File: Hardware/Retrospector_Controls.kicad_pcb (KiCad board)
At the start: 2 copper layers, 60 x 110 mm, 23 parts, among them J1 Audio_In_L, J10 Feedback_CV, J11 Audio_In_R, J12 Audio_Out_R, J13 Audio_Out_L, J2 Delay_CV_L, J3 Conn_01x08_Female, J4 Conn_01x08_Female, J5 Conn_01x08_Female, J6 Conn_01x08_Female, J7 Mix_CV, J8 Delay_CV_R, J9 Clock

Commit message: Renamed project files; work on panel PCB and 3d Models
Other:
- board text added: "Retrospector Controls v1 Mountjoy Modular"
- board text removed: "Alligator Controls v1 Mountjoy Modular"
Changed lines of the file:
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@@
   )
   (gr_line (start 130 50) (end 130 160) (layer Dwgs.User) (width 0.05))
-  (gr_text "Alligator Controls v1\nMountjoy Modular" (at 130.9 53.6) (layer B.SilkS)
+  (gr_text "Retrospector Controls v1\nMountjoy Modular" (at 130.9 53.6) (layer B.SilkS)
     (effects (font (size 1.5 1.5) (thickness 0.3)) (justify mirror))
   )

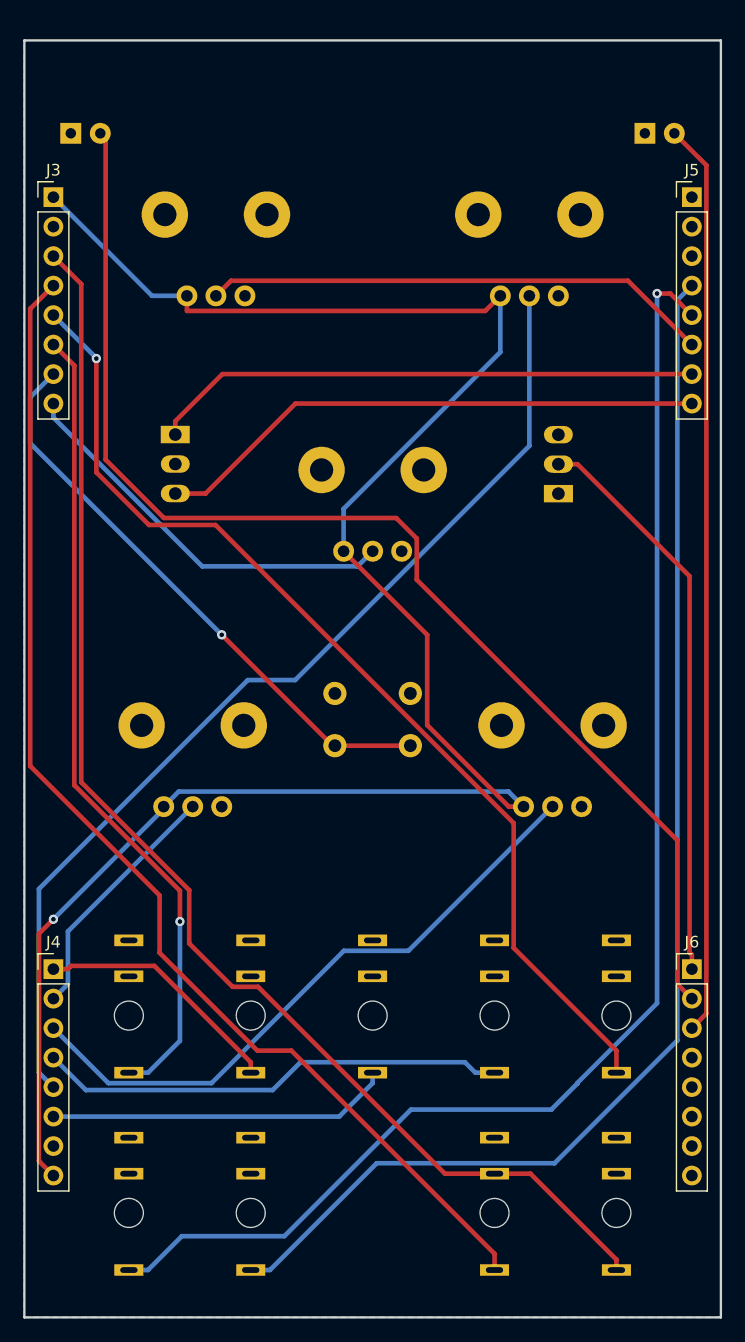
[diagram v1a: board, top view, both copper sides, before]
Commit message: Panel and Control PCB Updates
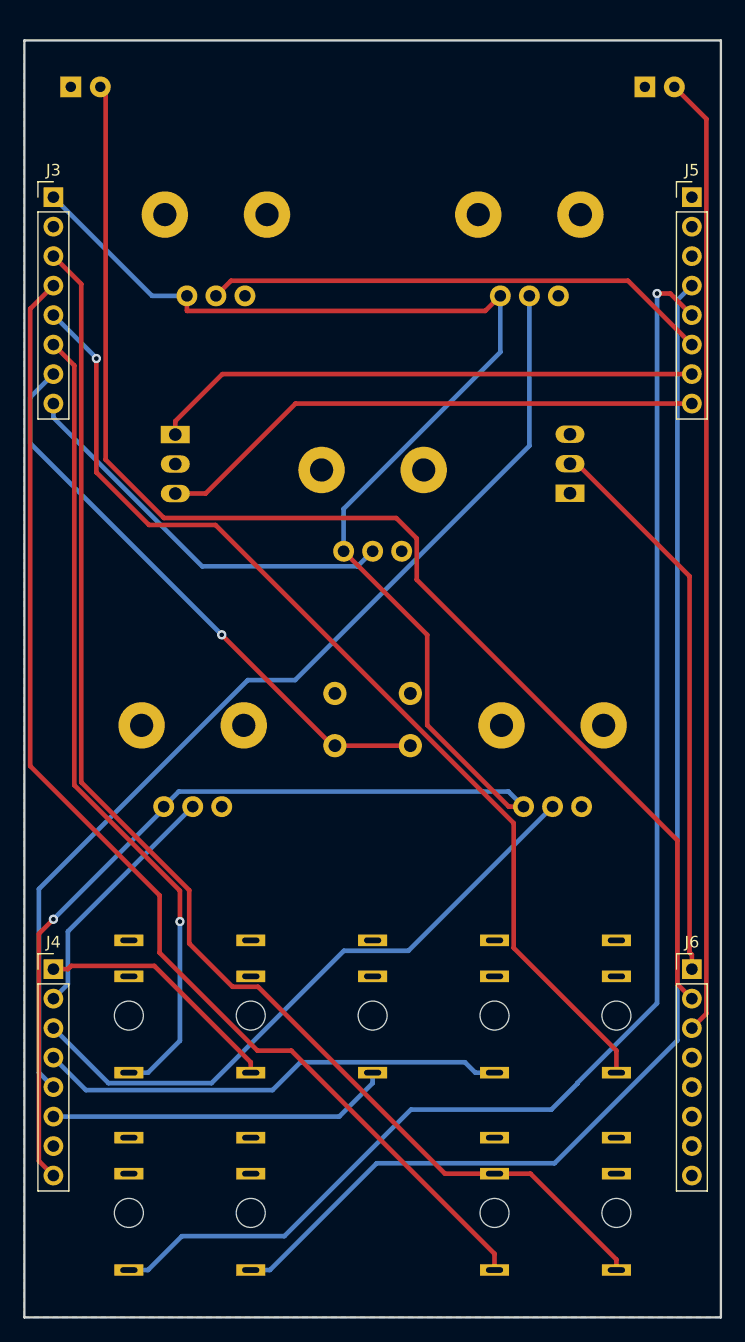
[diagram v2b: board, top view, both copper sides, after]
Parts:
- moved D1 4.00 mm to (153.4, 54.0)
- moved D2 4.00 mm to (104.0, 54.0)
- moved FXTYPE1 1.00 mm to (147.0, 89.0)
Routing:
- net /LED2: track 107.4 -> 112.4 mm
- net /LED1: track 78.7 -> 82.7 mm
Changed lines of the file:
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@@
     (thickness 1.6)
     (drawings 6)
-    (tracks 141)
+    (tracks 143)
     (zones 0)
     (modules 23)
@@
   )
   (module Custom_Footprints:SPDTSubMiniature (layer B.Cu)
-    (at 146 89.04 90)
+    (at 147 89 90)
     (descr "SPDT Sub Miniature Switch")
     (tags "Switch SPDT")
@@
   )
   (module LEDs:LED_D3.0mm (layer B.Cu)
-    (at 104 58)
+    (at 104 54)
     (descr "LED, diameter 3.0mm, 2 pins")
     (tags "LED diameter 3.0mm 2 pins")
@@
   )
   (module LEDs:LED_D3.0mm (layer B.Cu)
-    (at 153.45 58)
+    (at 153.45 54)
     (descr "LED, diameter 3.0mm, 2 pins")
     (tags "LED diameter 3.0mm 2 pins")
@@
   (segment (start 133.079999 128.420001) (end 127.522001 128.420001) (width 0.4) (layer B.Cu) (net 22))
   (segment (start 145.5 116) (end 133.079999 128.420001) (width 0.4) (layer B.Cu) (net 22) (status 10))
-  (segment (start 158.750001 133.829999) (end 157.5 135.08) (width 0.4) (layer F.Cu) (net 23) (status 20))
-  (segment (start 155.99 58) (end 158.750001 60.750001) (width 0.4) (layer F.Cu) (net 23) (status 10))
-  (segment (start 158.750001 60.750001) (end 158.750001 133.829999) (width 0.4) (layer F.Cu) (net 23))
-  (segment (start 107.000001 58.460001) (end 106.54 58) (width 0.4) (layer F.Cu) (net 24) (status 30))
-  (segment (start 107.000001 86.11416) (end 107.000001 58.460001) (width 0.4) (layer F.Cu) (net 24) (status 20))
+  (segment (start 158.750001 133.829999) (end 157.5 135.08) (width 0.4) (layer F.Cu) (net 23))
+  (segment (start 155.99 54) (end 158.750001 56.760001) (width 0.4) (layer F.Cu) (net 23))
+  (segment (start 158.750001 56.760001) (end 158.750001 133.829999) (width 0.4) (layer F.Cu) (net 23))
+  (segment (start 106.54 54) (end 107 54) (width 0.4) (layer F.Cu) (net 24))
+  (segment (start 106.54 54) (end 106.54 54.54) (width 0.4) (layer F.Cu) (net 24))
+  (segment (start 107.000001 86.11416) (end 107.000001 54.460001) (width 0.4) (layer F.Cu) (net 24))
+  (segment (start 112.023651 91.13781) (end 107.000001 86.11416) (width 0.4) (layer F.Cu) (net 24))
   (segment (start 132.03781 91.13781) (end 112.023651 91.13781) (width 0.4) (layer F.Cu) (net 24))
-  (segment (start 157.5 132.54) (end 156.249999 131.289999) (width 0.4) (layer F.Cu) (net 24) (status 10))
+  (segment (start 156.249999 131.289999) (end 156.249999 118.902001) (width 0.4) (layer F.Cu) (net 24))
+  (segment (start 107.000001 54.460001) (end 106.54 54) (width 0.4) (layer F.Cu) (net 24))
+  (segment (start 157.5 132.54) (end 156.249999 131.289999) (width 0.4) (layer F.Cu) (net 24))
+  (segment (start 133.800001 92.900001) (end 132.03781 91.13781) (width 0.4) (layer F.Cu) (net 24))
   (segment (start 156.249999 118.902001) (end 133.800001 96.452003) (width 0.4) (layer F.Cu) (net 24))
-  (segment (start 112.023651 91.13781) (end 107.000001 86.11416) (width 0.4) (layer F.Cu) (net 24))
-  (segment (start 133.800001 92.900001) (end 132.03781 91.13781) (width 0.4) (layer F.Cu) (net 24))
-  (segment (start 156.249999 131.289999) (end 156.249999 118.902001) (width 0.4) (layer F.Cu) (net 24))
   (segment (start 133.800001 96.452003) (end 133.800001 92.900001) (width 0.4) (layer F.Cu) (net 24))
   (segment (start 115.31792 95.300001) (end 102.5 82.482081) (width 0.4) (layer B.Cu) (net 25))

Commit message: Final changes to PCBs for manufacture
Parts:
- moved Delay_Pot_L1 0.50 mm to (141.5, 72.0)
- moved Delay_Pot_R1 0.50 mm to (113.5, 72.0)
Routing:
- net /DELAY_POT_R: track 43.8 -> 44.3 mm
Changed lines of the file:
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@@
       (drillshape 0)
       (scaleselection 1)
-      (outputdirectory "Gerbers/Components/"))
+      (outputdirectory "Gerbers/Controls/"))
   )
   (net 0 "")
@@
   )
   (module Custom_Footprints:Alpha_9mm_Potentiometer (layer B.Cu)
-    (at 114 72 90)
+    (at 113.5 72 90)
     (descr "Potentiometer, horizontally mounted, Omeg PC16PU, Omeg PC16PU, Omeg PC16PU, Vishay/Spectrol 248GJ/249GJ Single, Vishay/Spectrol 248GJ/249GJ Single, Vishay/Spectrol 248GJ/249GJ Single, Vishay/Spectrol 248GH/249GH Single, Vishay/Spectrol 148/149 Single, Vishay/Spectrol 148/149 Single, Vishay/Spectrol 148/149 Single, Vishay/Spectrol 148A/149A Single with mounting plates, Vishay/Spectrol 148/149 Double, Vishay/Spectrol 148A/149A Double with mounting plates, Piher PC-16 Single, Piher PC-16 Single, Piher PC-16 Single, Piher PC-16SV Single, Piher PC-16 Double, Piher PC-16 Triple, Piher T16H Single, Piher T16L Single, Piher T16H Double, Alps RK163 Single, Alps RK163 Double, Alps RK097 Single, Alps RK097 Double, Bourns PTV09A-2 Single with mounting sleve Single, Bourns PTV09A-1 with mounting sleve Single, Bourns PRS11S Single, Alps RK09K Single with mounting sleve Single, Alps RK09K with mounting sleve Single, http://www.alps.com/prod/info/E/HTML/Potentiometer/RotaryPotentiometers/RK09K/RK09D1130C1B.html")
     (tags "Potentiometer horizontal  Omeg PC16PU  Omeg PC16PU  Omeg PC16PU  Vishay/Spectrol 248GJ/249GJ Single  Vishay/Spectrol 248GJ/249GJ Single  Vishay/Spectrol 248GJ/249GJ Single  Vishay/Spectrol 248GH/249GH Single  Vishay/Spectrol 148/149 Single  Vishay/Spectrol 148/149 Single  Vishay/Spectrol 148/149 Single  Vishay/Spectrol 148A/149A Single with mounting plates  Vishay/Spectrol 148/149 Double  Vishay/Spectrol 148A/149A Double with mounting plates  Piher PC-16 Single  Piher PC-16 Single  Piher PC-16 Single  Piher PC-16SV Single  Piher PC-16 Double  Piher PC-16 Triple  Piher T16H Single  Piher T16L Single  Piher T16H Double  Alps RK163 Single  Alps RK163 Double  Alps RK097 Single  Alps RK097 Double  Bourns PTV09A-2 Single with mounting sleve Single  Bourns PTV09A-1 with mounting sleve Single  Bourns PRS11S Single  Alps RK09K Single with mounting sleve Single  Alps RK09K with mounting sleve Single")
@@
   )
   (module Custom_Footprints:Alpha_9mm_Potentiometer (layer B.Cu)
-    (at 141 72 90)
+    (at 141.5 72 90)
     (descr "Potentiometer, horizontally mounted, Omeg PC16PU, Omeg PC16PU, Omeg PC16PU, Vishay/Spectrol 248GJ/249GJ Single, Vishay/Spectrol 248GJ/249GJ Single, Vishay/Spectrol 248GJ/249GJ Single, Vishay/Spectrol 248GH/249GH Single, Vishay/Spectrol 148/149 Single, Vishay/Spectrol 148/149 Single, Vishay/Spectrol 148/149 Single, Vishay/Spectrol 148A/149A Single with mounting plates, Vishay/Spectrol 148/149 Double, Vishay/Spectrol 148A/149A Double with mounting plates, Piher PC-16 Single, Piher PC-16 Single, Piher PC-16 Single, Piher PC-16SV Single, Piher PC-16 Double, Piher PC-16 Triple, Piher T16H Single, Piher T16L Single, Piher T16H Double, Alps RK163 Single, Alps RK163 Double, Alps RK097 Single, Alps RK097 Double, Bourns PTV09A-2 Single with mounting sleve Single, Bourns PTV09A-1 with mounting sleve Single, Bourns PRS11S Single, Alps RK09K Single with mounting sleve Single, Alps RK09K with mounting sleve Single, http://www.alps.com/prod/info/E/HTML/Potentiometer/RotaryPotentiometers/RK09K/RK09D1130C1B.html")
     (tags "Potentiometer horizontal  Omeg PC16PU  Omeg PC16PU  Omeg PC16PU  Vishay/Spectrol 248GJ/249GJ Single  Vishay/Spectrol 248GJ/249GJ Single  Vishay/Spectrol 248GJ/249GJ Single  Vishay/Spectrol 248GH/249GH Single  Vishay/Spectrol 148/149 Single  Vishay/Spectrol 148/149 Single  Vishay/Spectrol 148/149 Single  Vishay/Spectrol 148A/149A Single with mounting plates  Vishay/Spectrol 148/149 Double  Vishay/Spectrol 148A/149A Double with mounting plates  Piher PC-16 Single  Piher PC-16 Single  Piher PC-16 Single  Piher PC-16SV Single  Piher PC-16 Double  Piher PC-16 Triple  Piher T16H Single  Piher T16L Single  Piher T16H Double  Alps RK163 Single  Alps RK163 Double  Alps RK097 Single  Alps RK097 Double  Bourns PTV09A-2 Single with mounting sleve Single  Bourns PTV09A-1 with mounting sleve Single  Bourns PRS11S Single  Alps RK09K Single with mounting sleve Single  Alps RK09K with mounting sleve Single")
@@
   (segment (start 134.700001 108.972793) (end 134.700001 101.200001) (width 0.4) (layer F.Cu) (net 2))
   (segment (start 143 116) (end 141.727208 116) (width 0.4) (layer F.Cu) (net 2) (status 10))
-  (segment (start 141 76.847998) (end 141 72) (width 0.4) (layer B.Cu) (net 2) (status 20))
-  (segment (start 127.5 90.347998) (end 141 76.847998) (width 0.4) (layer B.Cu) (net 2))
-  (segment (start 127.5 94) (end 127.5 90.347998) (width 0.4) (layer B.Cu) (net 2) (status 10))
   (segment (start 101.249999 126.950001) (end 102.5 125.7) (width 0.4) (layer F.Cu) (net 2))
   (segment (start 102.5 147.78) (end 101.249999 146.529999) (width 0.4) (layer F.Cu) (net 2) (status 10))
@@
   (segment (start 111 72) (end 102.5 63.5) (width 0.4) (layer B.Cu) (net 2) (status 20))
   (segment (start 114 72) (end 111 72) (width 0.4) (layer B.Cu) (net 2) (status 10))
-  (segment (start 114.027209 73.300001) (end 139.699999 73.300001) (width 0.4) (layer F.Cu) (net 2))
-  (segment (start 139.699999 73.300001) (end 141 72) (width 0.4) (layer F.Cu) (net 2) (status 20))
-  (segment (start 114 73.272792) (end 114.027209 73.300001) (width 0.4) (layer F.Cu) (net 2))
-  (segment (start 114 72) (end 114 73.272792) (width 0.4) (layer F.Cu) (net 2) (status 10))
   (segment (start 113.300001 114.699999) (end 112 116) (width 0.4) (layer B.Cu) (net 2) (status 20))
   (segment (start 141.699999 114.699999) (end 113.300001 114.699999) (width 0.4) (layer B.Cu) (net 2))
   (segment (start 143 116) (end 141.699999 114.699999) (width 0.4) (layer B.Cu) (net 2) (status 10))
+  (segment (start 139.699999 73.300001) (end 141 72) (width 0.4) (layer F.Cu) (net 2))
+  (segment (start 114.027209 73.300001) (end 139.699999 73.300001) (width 0.4) (layer F.Cu) (net 2))
+  (segment (start 113.5 72) (end 113.5 72.772792) (width 0.4) (layer F.Cu) (net 2))
+  (segment (start 113.5 72.772792) (end 114.027209 73.300001) (width 0.4) (layer F.Cu) (net 2))
+  (segment (start 141.5 72) (end 141.5 76.347998) (width 0.4) (layer B.Cu) (net 2))
+  (segment (start 127.5 90.347998) (end 127.5 94) (width 0.4) (layer B.Cu) (net 2))
+  (segment (start 141.5 76.347998) (end 127.5 90.347998) (width 0.4) (layer B.Cu) (net 2))
   (segment (start 157.5 128.75) (end 157.5 130) (width 0.4) (layer F.Cu) (net 3) (status 20))
   (segment (start 157.3 96.15) (end 157.3 128.55) (width 0.4) (layer F.Cu) (net 3))
@@
   (segment (start 116.465818 91.73782) (end 110.73782 91.73782) (width 0.4) (layer F.Cu) (net 15))
   (segment (start 142.150001 117.422003) (end 116.465818 91.73782) (width 0.4) (layer F.Cu) (net 15))
-  (segment (start 102.5 140.16) (end 101.249999 138.909999) (width 0.4) (layer B.Cu) (net 16) (status 10))
-  (segment (start 101.249999 123.097999) (end 119.247999 105.099999) (width 0.4) (layer B.Cu) (net 16))
-  (segment (start 143.5 84.924002) (end 143.5 72) (width 0.4) (layer B.Cu) (net 16) (status 20))
-  (segment (start 119.247999 105.099999) (end 123.324003 105.099999) (width 0.4) (layer B.Cu) (net 16))
-  (segment (start 101.249999 138.909999) (end 101.249999 123.097999) (width 0.4) (layer B.Cu) (net 16))
-  (segment (start 123.324003 105.099999) (end 143.5 84.924002) (width 0.4) (layer B.Cu) (net 16))
+  (segment (start 101.249999 138.909999) (end 102.5 140.16) (width 0.4) (layer B.Cu) (net 16))
+  (segment (start 144 84.424002) (end 123.324003 105.099999) (width 0.4) (layer B.Cu) (net 16))
+  (segment (start 144 72) (end 144 84.424002) (width 0.4) (layer B.Cu) (net 16))
+  (segment (start 123.324003 105.099999) (end 119.247999 105.099999) (width 0.4) (layer B.Cu) (net 16))
+  (segment (start 119.247999 105.099999) (end 101.249999 123.097999) (width 0.4) (layer B.Cu) (net 16))
+  (segment (start 101.249999 123.097999) (end 101.249999 138.909999) (width 0.4) (layer B.Cu) (net 16))
   (via (at 113.4 125.9) (size 0.8) (drill 0.4) (layers F.Cu B.Cu) (net 17))
   (segment (start 104.29999 77.99999) (end 102.5 76.2) (width 0.4) (layer F.Cu) (net 17) (status 20))
@@
   (segment (start 109 138.92) (end 110.65 138.92) (width 0.4) (layer B.Cu) (net 17) (status 10))
   (segment (start 110.65 138.92) (end 113.4 136.17) (width 0.4) (layer B.Cu) (net 17))
-  (segment (start 117.800001 70.699999) (end 116.5 72) (width 0.4) (layer F.Cu) (net 18) (status 20))
-  (segment (start 151.999999 70.699999) (end 117.800001 70.699999) (width 0.4) (layer F.Cu) (net 18))
-  (segment (start 157.5 76.2) (end 151.999999 70.699999) (width 0.4) (layer F.Cu) (net 18) (status 10))
+  (segment (start 151.999999 70.699999) (end 157.5 76.2) (width 0.4) (layer F.Cu) (net 18))
+  (segment (start 116 72) (end 117.300001 70.699999) (width 0.4) (layer F.Cu) (net 18))
+  (segment (start 117.300001 70.699999) (end 151.999999 70.699999) (width 0.4) (layer F.Cu) (net 18))
   (segment (start 103.750001 126.749999) (end 114.5 116) (width 0.4) (layer B.Cu) (net 19) (status 20))
   (segment (start 103.750001 131.289999) (end 103.750001 126.749999) (width 0.4) (layer B.Cu) (net 19))

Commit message: Updates to control and panel PCBs
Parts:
- removed FXTYPE1: SW_SPST, Custom_Footprints:SPDTSubMiniature
- added C1: 47uF, Capacitors_SMD:CP_Elec_5x5.8, F.Cu at (146.8, 54.2)
- added D3: LED_RGBA, Custom_Footprints:LED_RGB_PLCC4, B.Cu at (130.0, 102.2)
- added FILTER_MODE1: SW_SPDT_MSM, Custom_Footprints:SPDT_SubMiniature_Aligned, B.Cu at (130.1, 110.3)
- added J14: Filter, Custom_Footprints:THONKICONN_hole, B.Cu at (130.1, 127.1)
- added LOCK1: SW_Push, Custom_Footprints:SW_PUSH_6mm_aligned, B.Cu at (130.1, 65.6)
- added R1: 3k3, Resistors_SMD:R_0603_HandSoldering, F.Cu at (133.9, 51.5)
- added R2: 3k3, Resistors_SMD:R_0603_HandSoldering, F.Cu at (128.3, 51.0)
- added R3: 3k3, Resistors_SMD:R_0603_HandSoldering, F.Cu at (122.2, 51.3)
- added U1: TB62781FNG, Housings_SSOP:SSOP-20_4.4x6.5mm_Pitch0.65mm, F.Cu at (130.0, 57.3)
- added WIDTH_MODE1: SW_SPDT_MSM, Custom_Footprints:SPDT_SubMiniature_Aligned, B.Cu at (146.3, 86.5)
- D1, D2: value LED -> LED_RGBA; footprint LEDs:LED_D3.0mm -> Custom_Footprints:LED_RGB_PLCC4
- DELAY_MODE1: renamed from FXMODE1; footprint Custom_Footprints:SPDTSubMiniature -> Custom_Footprints:SPDT_SubMiniature_Aligned
- Delay_Pot_L1, Delay_Pot_R1, Feedback_Pot1, Mix_Pot1, Tone_Pot1: value A10k -> B10k; footprint Custom_Footprints:Alpha_9mm_Potentiometer -> Custom_Footprints:Alpha_9mm_Potentiometer_Aligned
- RESET1: footprint Buttons_Switches_THT:SW_PUSH_6mm -> Custom_Footprints:SW_PUSH_6mm_aligned
- moved RESET1 27.8 mm to (130.0, 138.4)
- moved J9 17.0 mm to (130.0, 151.0)
- moved Delay_Pot_L1 8.50 mm to (145.5, 64.5), turned to 180 degrees
- moved Feedback_Pot1 7.91 mm to (145.5, 108.5), turned to 180 degrees
- moved Mix_Pot1 7.91 mm to (114.5, 108.5), turned to 180 degrees
- moved Tone_Pot1 7.91 mm to (130.0, 86.5), turned to 180 degrees
- moved Delay_Pot_R1 7.57 mm to (114.5, 64.5), turned to 180 degrees
- moved DELAY_MODE1 2.55 mm to (113.0, 86.5)
- moved D1 1.45 mm to (154.9, 53.9)
- moved D2 1.30 mm to (105.3, 54.0)
- renumbered J3 to J1, J5 to J2, J4 to J3, J6 to J4, J1 to J5, J2 to J6
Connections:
- net /TONE_POT renamed /FILTER_POT
- D1 pad 1: GND -> Net-(D1-Pad1)
- D1 pad 2: /LED1 -> Net-(D1-Pad2)
- D2 pad 1: GND -> Net-(D2-Pad1)
- D2 pad 2: /LED2 -> Net-(D2-Pad2)
- J1 pad 3: /EXT_AUDIO_IN_L -> /DELAY_CV_L
- J1 pad 4: /EXT_AUDIO_IN_R -> /DELAY_CV_R
- J1 pad 5: /DELAY_CV_L -> /EXT_AUDIO_IN_L
- J1 pad 6: /DELAY_CV_R -> /EXT_AUDIO_IN_R
- J1 pad 7: /RESET -> /DELAY_POT_R
- J2 pad 1: GND -> +5V
- J2 pad 2: GND -> +3V3
- J2 pad 4: /EXT_AUDIO_OUT_L -> /MODE1
- J2 pad 5: /EXT_AUDIO_OUT_R -> /MODE2
- J2 pad 6: /DELAY_POT_R -> /RESET
- J2 pad 7: /MODE1 -> /EXT_AUDIO_OUT_L
- J2 pad 8: /MODE2 -> /EXT_AUDIO_OUT_R
- J3 pad 1: /MIX_CV -> /CLOCK
- J3 pad 3: /FEEDBACK_POT -> /MIX_CV
- J3 pad 4: /FEEDBACK_CV -> /FEEDBACK_POT
- J3 pad 5: /DELAY_POT_L -> /FILTER_CV
- J3 pad 6: /CLOCK -> /DELAY_POT_L
- J3 pad 7: GND -> /FEEDBACK_CV
- J3 pad 8: +3.3VA -> GND
- J4 pad 1: /DELAY_CHORUS -> /LED_SPI_DATA
- J4 pad 2: /LED2 -> /LED_SPI_CLK
- J4 pad 3: /LED1 -> /LINK_BTN
- J4 pad 4: /USB_DP -> /PINGPONG
- J4 pad 5: /USB_DM -> /CHORUS
- J4 pad 6: /USB_VBUS -> /HP_MODE
- J4 pad 7: GND -> /LP_MODE
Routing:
- net +3.3VA: track 169.8 -> 0.00 mm, vias 1 -> 0
- net /EXT_AUDIO_OUT_R: track 120.0 -> 0.00 mm, vias 1 -> 0
- net /EXT_AUDIO_IN_L: track 113.0 -> 0.00 mm
- net /LED2: track 112.4 -> 0.00 mm
- net /EXT_AUDIO_OUT_L: track 110.5 -> 0.00 mm
- net /EXT_AUDIO_IN_R: track 103.9 -> 0.00 mm
- net /DELAY_POT_L: track 88.8 -> 0.00 mm
- net /DELAY_CV_L: track 88.7 -> 0.00 mm, vias 1 -> 0
- net /LED1: track 82.7 -> 0.00 mm
- net /DELAY_CV_R: track 70.0 -> 0.00 mm, vias 1 -> 0
- net /FEEDBACK_POT: track 54.8 -> 0.00 mm
- net /RESET: track 50.5 -> 0.00 mm, vias 1 -> 0
- net /DELAY_CHORUS: track 49.2 -> 0.00 mm
- net /MODE2: track 47.7 -> 0.00 mm
- net /MODE1: track 47.3 -> 0.00 mm
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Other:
- board text added: "Retrospector Controls v2 Mountjoy Modular"
- board text removed: "Retrospector Controls v1 Mountjoy Modular"
